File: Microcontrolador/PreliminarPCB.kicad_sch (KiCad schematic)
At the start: 8 parts, among them J1 Conn_01x20_Female, J2 Conn_01x20_Female, J3 Conn_01x08_Pin, SW1 SW_Push, SW2 SW_Push, SW3 SW_Push, SW4 SW_Push, SW5 SW_Push

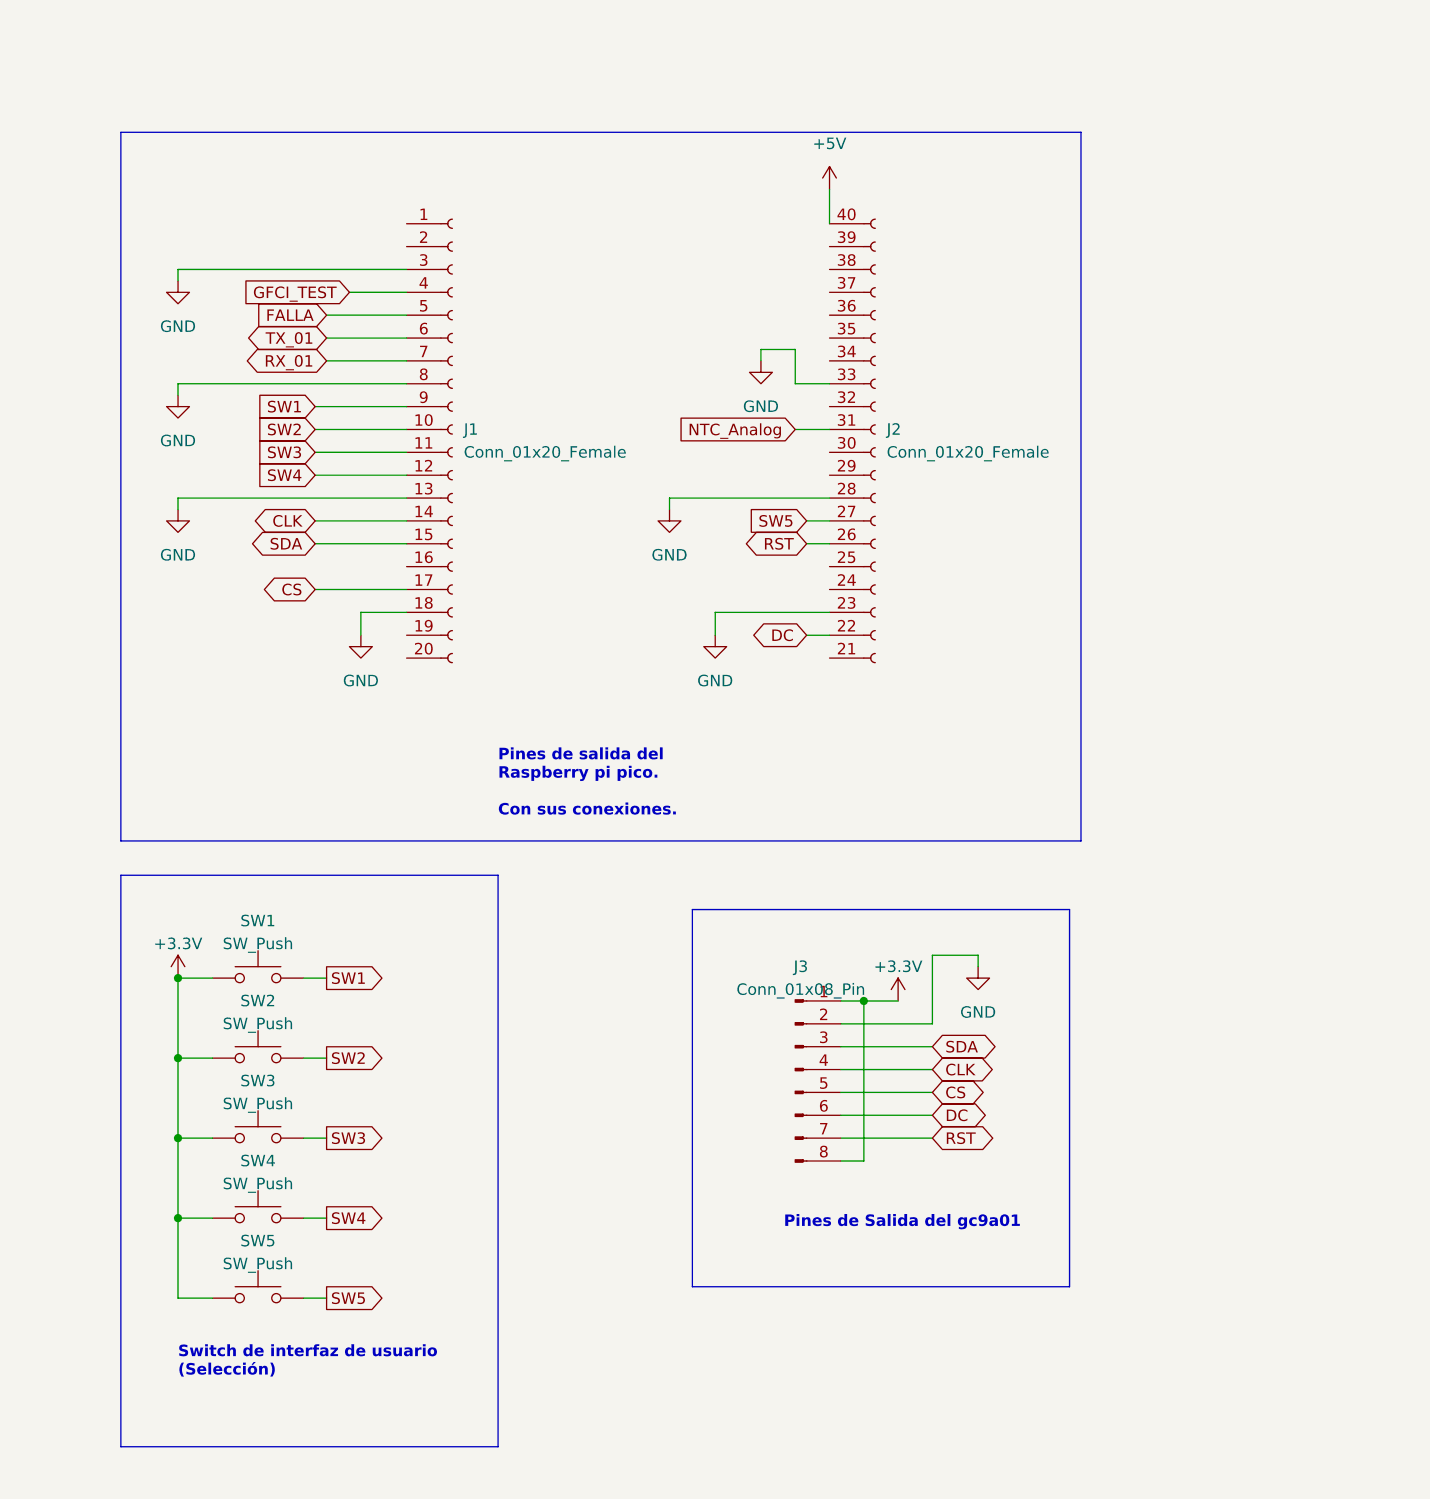
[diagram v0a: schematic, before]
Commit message: actualización huella rp2040
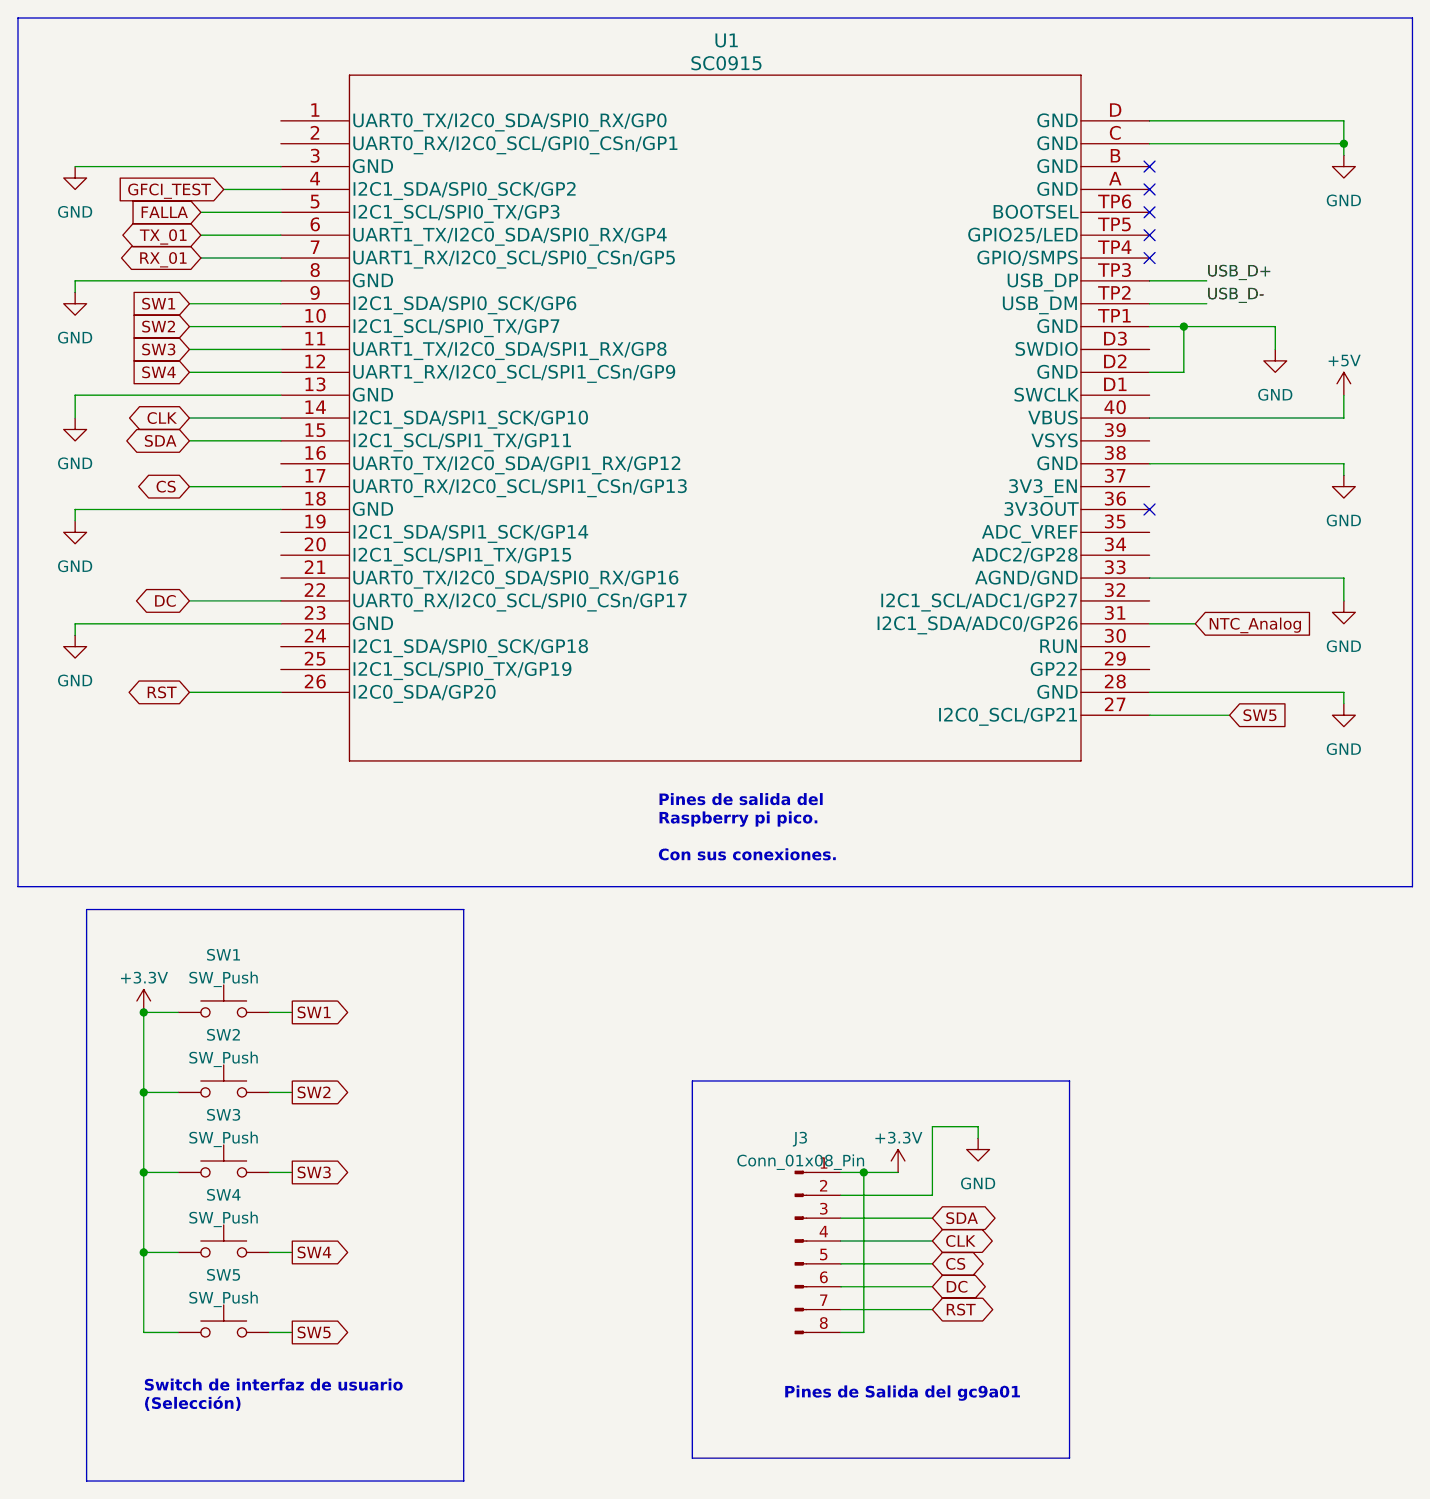
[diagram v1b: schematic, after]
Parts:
- removed J1, J2: Conn_01x20_Female, symbol Connector:Conn_01x20_Female
- added U1: SC0915, SC0915_RPI, symbol RP2040:SC0915
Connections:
- net +5V: now also U1.40 (VBUS)
- net CLK: now also U1.14 (I2C1_SDA/SPI1_SCK/GP10)
- net CS: now also U1.17 (UART0_RX/I2C0_SCL/SPI1_CSn/GP13)
- net DC: now also U1.22 (UART0_RX/I2C0_SCL/SPI0_CSn/GP17)
- net FALLA: now also U1.5 (I2C1_SCL/SPI0_TX/GP3)
- net GFCI_TEST: now also U1.4 (I2C1_SDA/SPI0_SCK/GP2)
- net GND: now also U1.13 (GND), U1.18 (GND), U1.23 (GND), U1.28 (GND), U1.3 (GND), U1.33 (AGND/GND), U1.38 (GND), U1.8 (GND), U1.C (GND), U1.D (GND), U1.D2 (GND), U1.TP1 (GND)
- net NTC_Analog: now also U1.31 (I2C1_SDA/ADC0/GP26)
- net RST: now also U1.26 (I2C0_SDA/GP20)
- net RX_01: now also U1.7 (UART1_RX/I2C0_SCL/SPI0_CSn/GP5)
- net SDA: now also U1.15 (I2C1_SCL/SPI1_TX/GP11)
- net SW1: now also U1.9 (I2C1_SDA/SPI0_SCK/GP6)
- net SW2: now also U1.10 (I2C1_SCL/SPI0_TX/GP7)
- net SW3: now also U1.11 (UART1_TX/I2C0_SDA/SPI1_RX/GP8)
- net SW4: now also U1.12 (UART1_RX/I2C0_SCL/SPI1_CSn/GP9)
- net SW5: now also U1.27 (I2C0_SCL/GP21)
- net TX_01: now also U1.6 (UART1_TX/I2C0_SDA/SPI0_RX/GP4)
- new net USB_D+: U1.TP3 (USB_DP)
- new net USB_D-: U1.TP2 (USB_DM)
- no-connect marks 0 -> 6
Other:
- moved on the sheet: J3, SW1, SW2, SW3, SW4, SW5

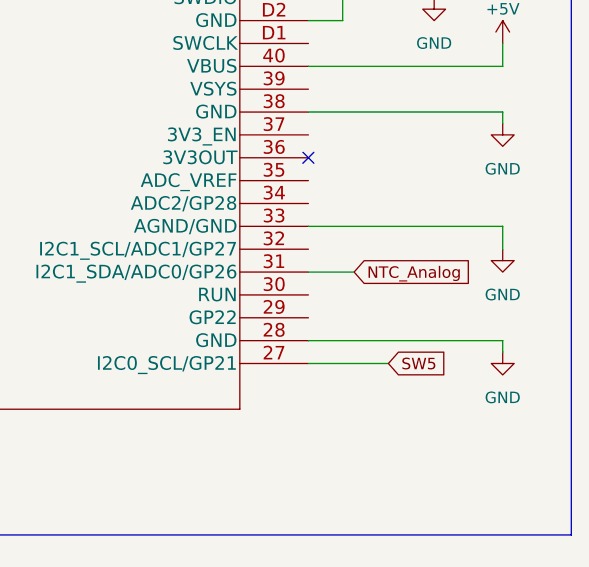
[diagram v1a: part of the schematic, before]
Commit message: correción de algunas referencias
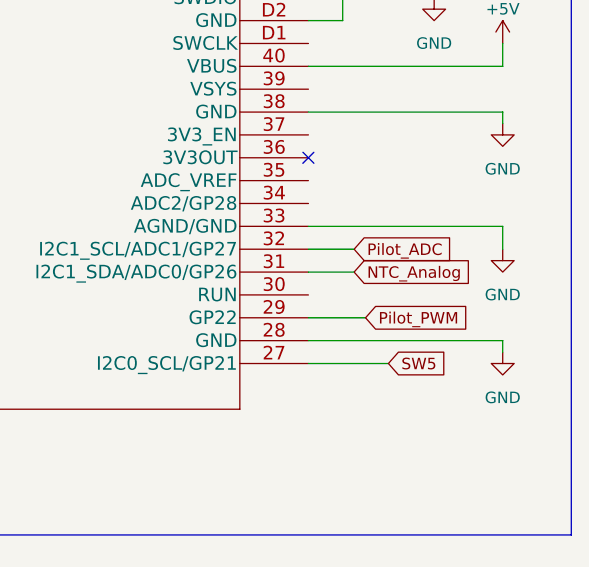
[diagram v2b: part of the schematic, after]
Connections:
- net Pilot_PWM: now reaches U1.29 (GP22)
- net Pilot_ADC: now reaches U1.32 (I2C1_SCL/ADC1/GP27)
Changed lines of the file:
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@@
+    (stroke (width 0) (type default))
+  )
+  (wire (pts (xy 139.7 78.74) (xy 144.78 78.74))
     (stroke (width 0) (type default))
   )
@@
   )
   (wire (pts (xy 139.7 88.9) (xy 161.29 88.9))
+    (stroke (width 0) (type default))
+  )
+  (wire (pts (xy 139.7 86.36) (xy 146.05 86.36))
     (stroke (width 0) (type default))
   )
@@
     )
   )
+  (global_label "Pilot_ADC" (shape input) (at 144.78 78.74 0) (fields_autoplaced)
+    (effects (font (size 1.27 1.27)) (justify left))
+    (property "Intersheetrefs" "${INTERSHEET_REFS}" (at 156.6967 78.74 0)
+      (effects (font (size 1.27 1.27)) (justify left) hide)
+    )
+  )
   (global_label "SW3" (shape output) (at 44.45 142.24 0) (fields_autoplaced)
     (effects (font (size 1.27 1.27)) (justify left))
@@
     )
   )
+  (global_label "Pilot_PWM" (shape input) (at 146.05 86.36 0) (fields_autoplaced)
+    (effects (font (size 1.27 1.27)) (justify left))
+    (property "Intersheetrefs" "${INTERSHEET_REFS}" (at 158.5109 86.36 0)
+      (effects (font (size 1.27 1.27)) (justify left) hide)
+    )
+  )
